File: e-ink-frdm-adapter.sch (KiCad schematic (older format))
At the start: 23 parts, among them P1 2-1734839-4, P2 68000-110HLF, Q1 MF-DSC-SOT233-BSS138

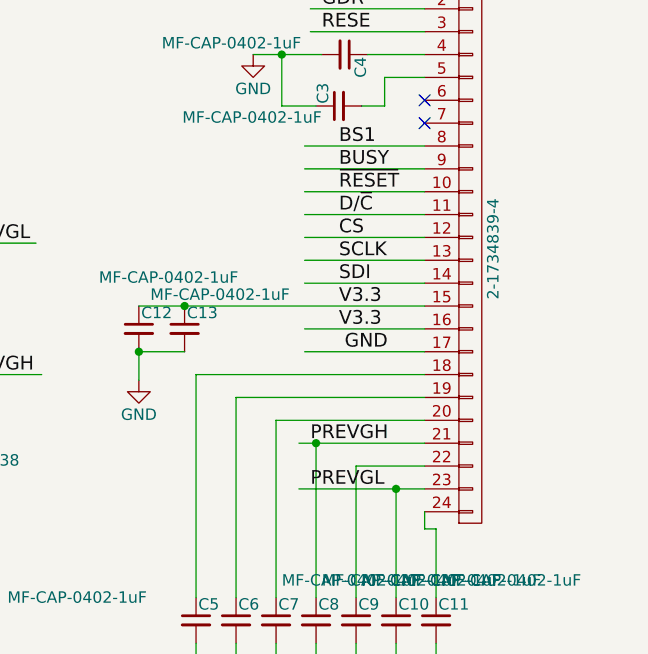
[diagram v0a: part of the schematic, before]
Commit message: Use bottom contact FPC conn footprint
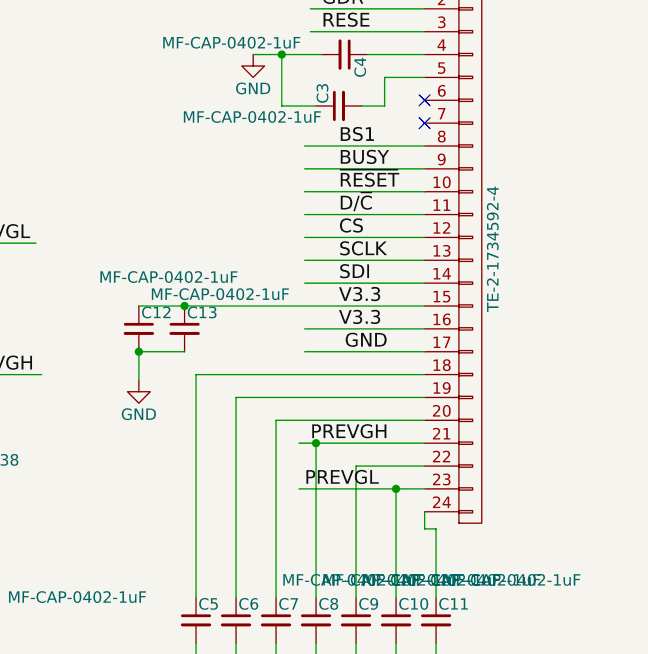
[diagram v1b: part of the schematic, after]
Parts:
- P1: value 2-1734839-4 -> TE-2-1734592-4; footprint muchi_footprints:TE-2-1734839-4 -> muchi_footprints:TE-2-1734592-4-bottom_contact
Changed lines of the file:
@@
 P 8075 3575
 F 0 "P1" H 8075 4825 50  0000 C CNN
-F 1 "2-1734839-4" V 8175 3575 50  0000 C CNN
-F 2 "muchi_footprints:TE-2-1734839-4" H 8075 3575 50  0001 C CNN
+F 1 "TE-2-1734592-4" V 8175 3575 50  0000 C CNN
+F 2 "muchi_footprints:TE-2-1734592-4-bottom_contact" H 8075 3575 50  0001 C CNN
 F 3 "" H 8075 3575 50  0000 C CNN
 	1    8075 3575
@@
 Text Label 5825 3550 0    60   ~ 0
 PREVGL
-Text Label 7375 4625 0    60   ~ 0
+Text Label 7350 4625 0    60   ~ 0
 PREVGL
 $Comp

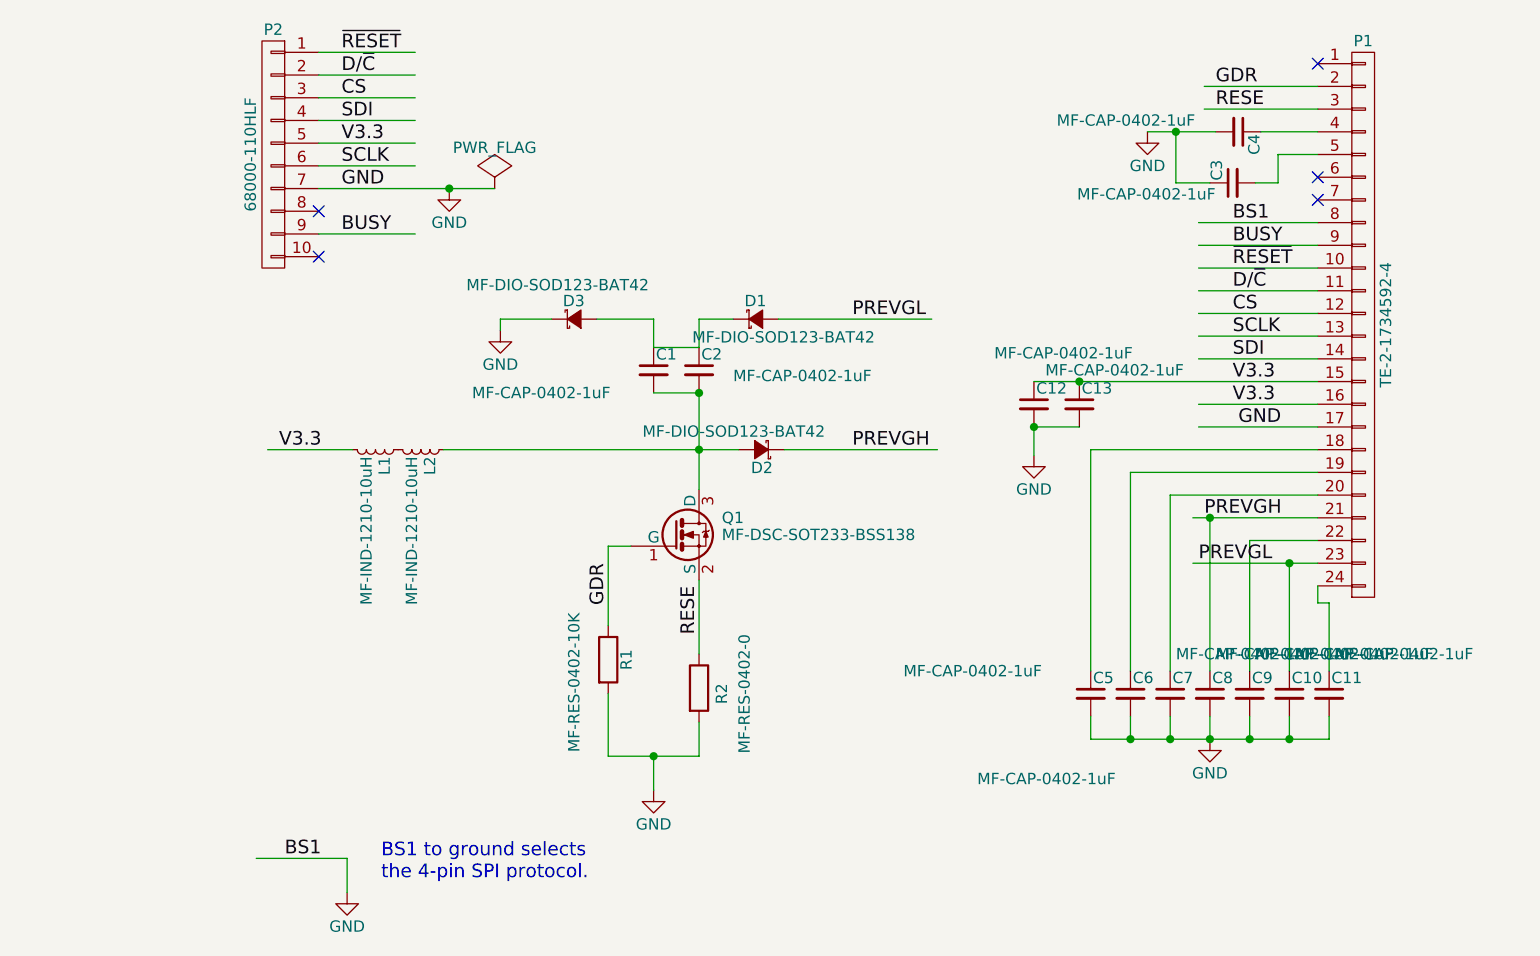
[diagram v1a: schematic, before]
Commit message: 1. P1 FPC connector changed from top contact to bottom contact. 2. C2, C13 reduced from 1uF to 0.1uF 3. C1, C12 need not be installed (DNI) 4. R2 from 0 OHM to 10 OHM
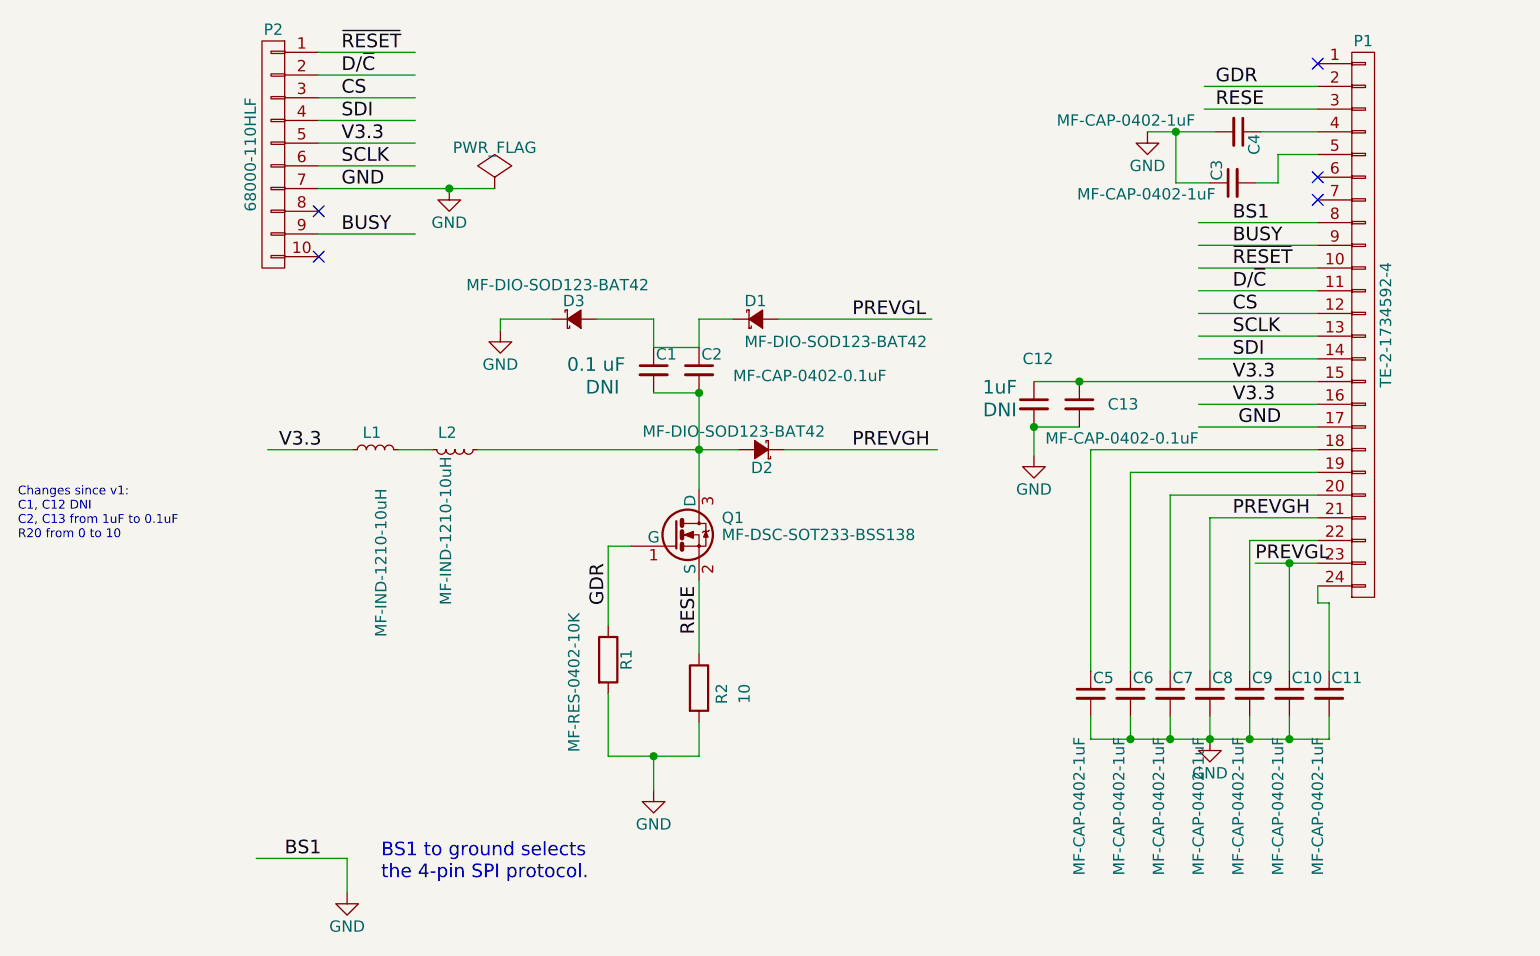
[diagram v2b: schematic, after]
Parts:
- C1: Install (none) -> DNI; Pretty Value (none) -> 0.1 uF
- C12: Install (none) -> DNI; Pretty Value (none) -> 1uF
- C13, C2: value MF-CAP-0402-1uF -> MF-CAP-0402-0.1uF
- R2: value MF-RES-0402-0 -> 10
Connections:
- wire segments 74 -> 75
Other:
- note added: "Changes since v1:\nC1, C12 DNI\nC2, C13 from 1uF to 0.1uF\nR20 from 0 to 10"
- moved on the sheet: L1, L2
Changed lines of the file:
@@
 $EndComp
 $Comp
-L GND #PWR01
+L GND #PWR6
 U 1 1 578976A8
 P 7125 2725
-F 0 "#PWR01" H 7125 2475 50  0001 C CNN
+F 0 "#PWR6" H 7125 2475 50  0001 C CNN
 F 1 "GND" H 7125 2575 50  0000 C CNN
 F 2 "" H 7125 2725 50  0000 C CNN
@@
 P 5150 5175
 F 0 "R2" V 5250 5150 50  0000 C CNN
-F 1 "MF-RES-0402-0" V 5350 5150 50  0000 C CNN
+F 1 "10" V 5350 5150 50  0000 C CNN
 F 2 "Resistors_SMD:R_0402" V 5080 5175 50  0001 C CNN
 F 3 "" H 5150 5175 50  0000 C CNN
@@
 Text Label 5825 4125 0    60   ~ 0
 PREVGH
-Text Label 7375 4425 0    60   ~ 0
+Text Label 7500 4425 0    60   ~ 0
 PREVGH
 $Comp
@@
 P 5150 3775
 F 0 "C2" H 5160 3845 50  0000 L CNN
-F 1 "MF-CAP-0402-1uF" H 5300 3750 50  0000 L CNN
+F 1 "MF-CAP-0402-0.1uF" H 5300 3750 50  0000 L CNN
 F 2 "Resistors_SMD:R_0402" H 5150 3775 50  0001 C CNN
 F 3 "" H 5150 3775 50  0000 C CNN
@@
 P 4950 3775
 F 0 "C1" H 4960 3845 50  0000 L CNN
-F 1 "MF-CAP-0402-1uF" H 4150 3675 50  0000 L CNN
+F 1 "MF-CAP-0402-1uF" H 4150 3675 50  0001 L CNN
 F 2 "Resistors_SMD:R_0402" H 4950 3775 50  0001 C CNN
 F 3 "" H 4950 3775 50  0000 C CNN
+F 4 "DNI" H 4725 3700 60  0000 C CNN "Install"
+F 5 "0.1 uF" H 4825 3800 60  0000 R CNN "Pretty Value"
 	1    4950 3775
 	1    0    0    -1
@@
 P 5400 3550
 F 0 "D1" H 5350 3630 50  0000 L CNN
-F 1 "MF-DIO-SOD123-BAT42" H 5120 3470 50  0000 L CNN
+F 1 "MF-DIO-SOD123-BAT42" H 5350 3450 50  0000 L CNN
 F 2 "Diodes_SMD:SOD-123" V 5400 3550 50  0001 C CNN
 F 3 "" V 5400 3550 50  0000 C CNN
@@
 Text Label 5825 3550 0    60   ~ 0
 PREVGL
-Text Label 7350 4625 0    60   ~ 0
+Text Label 7600 4625 0    60   ~ 0
 PREVGL
 $Comp
@@
 P 7400 5200
 F 0 "C8" H 7410 5270 50  0000 L CNN
-F 1 "MF-CAP-0402-1uF" H 7425 5375 50  0000 L CNN
+F 1 "MF-CAP-0402-1uF" V 7350 4400 50  0000 L CNN
 F 2 "Resistors_SMD:R_0402" H 7400 5200 50  0001 C CNN
 F 3 "" H 7400 5200 50  0000 C CNN
@@
 $EndComp
 $Comp
-L GND #PWR02
+L GND #PWR7
 U 1 1 57898799
 P 7400 5400
-F 0 "#PWR02" H 7400 5150 50  0001 C CNN
+F 0 "#PWR7" H 7400 5150 50  0001 C CNN
 F 1 "GND" H 7400 5250 50  0000 C CNN
 F 2 "" H 7400 5400 50  0000 C CNN
@@
 P 7575 5200
 F 0 "C9" H 7585 5270 50  0000 L CNN
-F 1 "MF-CAP-0402-1uF" H 7600 5375 50  0000 L CNN
+F 1 "MF-CAP-0402-1uF" V 7525 4400 50  0000 L CNN
 F 2 "Resistors_SMD:R_0402" H 7575 5200 50  0001 C CNN
 F 3 "" H 7575 5200 50  0000 C CNN
@@
 P 6875 5200
 F 0 "C5" H 6885 5270 50  0000 L CNN
-F 1 "MF-CAP-0402-1uF" H 6050 5300 50  0000 L CNN
+F 1 "MF-CAP-0402-1uF" V 6825 4400 50  0000 L CNN
 F 2 "Resistors_SMD:R_0402" H 6875 5200 50  0001 C CNN
 F 3 "" H 6875 5200 50  0000 C CNN
@@
 P 7050 5200
 F 0 "C6" H 7060 5270 50  0000 L CNN
-F 1 "MF-CAP-0402-1uF" H 6375 4825 50  0000 L CNN
+F 1 "MF-CAP-0402-1uF" V 7000 4400 50  0000 L CNN
 F 2 "Resistors_SMD:R_0402" H 7050 5200 50  0001 C CNN
 F 3 "" H 7050 5200 50  0000 C CNN
@@
 P 7225 5200
 F 0 "C7" H 7235 5270 50  0000 L CNN
-F 1 "MF-CAP-0402-1uF" H 7250 5375 50  0000 L CNN
+F 1 "MF-CAP-0402-1uF" V 7175 4400 50  0000 L CNN
 F 2 "Resistors_SMD:R_0402" H 7225 5200 50  0001 C CNN
 F 3 "" H 7225 5200 50  0000 C CNN
@@
 P 7750 5200
 F 0 "C10" H 7760 5270 50  0000 L CNN
-F 1 "MF-CAP-0402-1uF" H 7775 5375 50  0000 L CNN
+F 1 "MF-CAP-0402-1uF" V 7700 4400 50  0000 L CNN
 F 2 "Resistors_SMD:R_0402" H 7750 5200 50  0001 C CNN
 F 3 "" H 7750 5200 50  0000 C CNN
@@
 P 7925 5200
 F 0 "C11" H 7935 5270 50  0000 L CNN
-F 1 "MF-CAP-0402-1uF" H 7950 5375 50  0000 L CNN
+F 1 "MF-CAP-0402-1uF" V 7875 4400 50  0000 L CNN
 F 2 "Resistors_SMD:R_0402" H 7925 5200 50  0001 C CNN
 F 3 "" H 7925 5200 50  0000 C CNN
@@
 	4750 5475 5150 5475
 Wire Wire Line
-	4025 4125 5325 4125
-Wire Wire Line
 	5150 3875 5150 4300
 Connection ~ 5150 4125
 Wire Wire Line
 	5525 4125 6200 4125
-Wire Wire Line
-	7875 4425 7325 4425
 Connection ~ 5150 3875
 Wire Wire Line
@@
 Wire Wire Line
 	5500 3550 6175 3550
-Wire Wire Line
-	7875 4625 7325 4625
 Wire Wire Line
 	7875 4125 6875 4125
@@
 Wire Wire Line
 	7400 5100 7400 4425
-Connection ~ 7400 4425
 Wire Wire Line
 	7575 5100 7575 4525
@@
 	3600 5925 3600 6075
 $Comp
-L GND #PWR03
+L GND #PWR1
 U 1 1 57899AA0
 P 3600 6075
-F 0 "#PWR03" H 3600 5825 50  0001 C CNN
+F 0 "#PWR1" H 3600 5825 50  0001 C CNN
 F 1 "GND" H 3600 5925 50  0000 C CNN
 F 2 "" H 3600 6075 50  0000 C CNN
@@
 GND
 $Comp
-L GND #PWR04
+L GND #PWR2
 U 1 1 5789A5C5
 P 4050 2975
-F 0 "#PWR04" H 4050 2725 50  0001 C CNN
+F 0 "#PWR2" H 4050 2725 50  0001 C CNN
 F 1 "GND" H 4050 2825 50  0000 C CNN
 F 2 "" H 4050 2975 50  0000 C CNN
@@
 	6625 4025 6625 4150
 $Comp
-L GND #PWR05
+L GND #PWR5
 U 1 1 5789B0C3
 P 6625 4150
-F 0 "#PWR05" H 6625 3900 50  0001 C CNN
+F 0 "#PWR5" H 6625 3900 50  0001 C CNN
 F 1 "GND" H 6625 4000 50  0000 C CNN
 F 2 "" H 6625 4150 50  0000 C CNN
@@
 U 1 1 5789B5B1
 P 3725 4125
-F 0 "L1" H 3755 4165 50  0000 L CNN
-F 1 "MF-IND-1210-10uH" H 3755 4085 50  0000 L CNN
+F 0 "L1" V 3800 4100 50  0000 L CNN
+F 1 "MF-IND-1210-10uH" H 2900 4100 50  0000 L CNN
 F 2 "Resistors_SMD:R_1210" H 3725 4125 50  0001 C CNN
 F 3 "" H 3725 4125 50  0000 C CNN
 	1    3725 4125
-	0    1    1    0
+	0    -1   -1   0
 $EndComp
 $Comp
 L L_Small L2
 U 1 1 5789B675
-P 3925 4125
-F 0 "L2" H 3955 4165 50  0000 L CNN
-F 1 "MF-IND-1210-10uH" H 3955 4085 50  0000 L CNN
-F 2 "Resistors_SMD:R_1210" H 3925 4125 50  0001 C CNN
-F 3 "" H 3925 4125 50  0000 C CNN
-	1    3925 4125
+P 4075 4125
+F 0 "L2" V 4000 4050 50  0000 L CNN
+F 1 "MF-IND-1210-10uH" H 4105 4085 50  0000 L CNN
+F 2 "Resistors_SMD:R_1210" H 4075 4125 50  0001 C CNN
+F 3 "" H 4075 4125 50  0000 C CNN
+	1    4075 4125
 	0    1    1    0
 $EndComp
@@
 Connection ~ 4950 5475
 $Comp
-L GND #PWR06
+L GND #PWR4
 U 1 1 5789BD2A
 P 4950 5625
-F 0 "#PWR06" H 4950 5375 50  0001 C CNN
+F 0 "#PWR4" H 4950 5375 50  0001 C CNN
 F 1 "GND" H 4950 5475 50  0000 C CNN
 F 2 "" H 4950 5625 50  0000 C CNN
@@
 $EndComp
 $Comp
-L PWR_FLAG #FLG07
+L PWR_FLAG #FLG1
 U 1 1 5789BD68
 P 4250 2975
-F 0 "#FLG07" H 4250 3070 50  0001 C CNN
+F 0 "#FLG1" H 4250 3070 50  0001 C CNN
 F 1 "PWR_FLAG" H 4250 3155 50  0000 C CNN
 F 2 "" H 4250 2975 50  0000 C CNN
@@
 	4275 3550 4275 3600
 $Comp
-L GND #PWR08
+L GND #PWR3
 U 1 1 57899B0B
 P 4275 3600
-F 0 "#PWR08" H 4275 3350 50  0001 C CNN
+F 0 "#PWR3" H 4275 3350 50  0001 C CNN
 F 1 "GND" H 4275 3450 50  0000 C CNN
 F 2 "" H 4275 3600 50  0000 C CNN
@@
 U 1 1 5789E4D3
 P 6625 3925
-F 0 "C12" H 6635 3995 50  0000 L CNN
-F 1 "MF-CAP-0402-1uF" H 6450 4150 50  0000 L CNN
+F 0 "C12" H 6575 4125 50  0000 L CNN
+F 1 "MF-CAP-0402-1uF" H 6450 4150 50  0001 L CNN
 F 2 "Resistors_SMD:R_0402" H 6625 3925 50  0001 C CNN
 F 3 "" H 6625 3925 50  0000 C CNN
+F 4 "DNI" H 6475 3900 60  0000 C CNN "Install"
+F 5 "1uF" H 6475 4000 60  0000 C CNN "Pretty Value"
 	1    6625 3925
 	1    0    0    -1
@@
 U 1 1 5789E581
 P 6825 3925
-F 0 "C13" H 6835 3995 50  0000 L CNN
-F 1 "MF-CAP-0402-1uF" H 6675 4075 50  0000 L CNN
+F 0 "C13" H 6950 3925 50  0000 L CNN
+F 1 "MF-CAP-0402-0.1uF" H 6675 3775 50  0000 L CNN
 F 2 "Resistors_SMD:R_0402" H 6825 3925 50  0001 C CNN
 F 3 "" H 6825 3925 50  0000 C CNN
@@
 Connection ~ 6625 4025
 Connection ~ 6825 3825
+Wire Wire Line
+	7875 4625 7600 4625
+Wire Wire Line
+	7400 4425 7875 4425
+Text Notes 2150 4525 0    39   ~ 0
+Changes since v1:\nC1, C12 DNI\nC2, C13 from 1uF to 0.1uF\nR20 from 0 to 10
+Wire Wire Line
+	5325 4125 4175 4125
+Wire Wire Line
+	3975 4125 3825 4125
 $EndSCHEMATC
